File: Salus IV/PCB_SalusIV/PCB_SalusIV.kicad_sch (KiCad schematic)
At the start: 83 parts, among them J1 DC-005-5A-2.0, J2 DC-005-5A-2.0, Q1 IRFR5305TRPBF, Q2 IRFR5305TRPBF, Q3 IRFR5305TRPBF, Q4 IRFR5305TRPBF, Q9 IRLML6344TRPBF

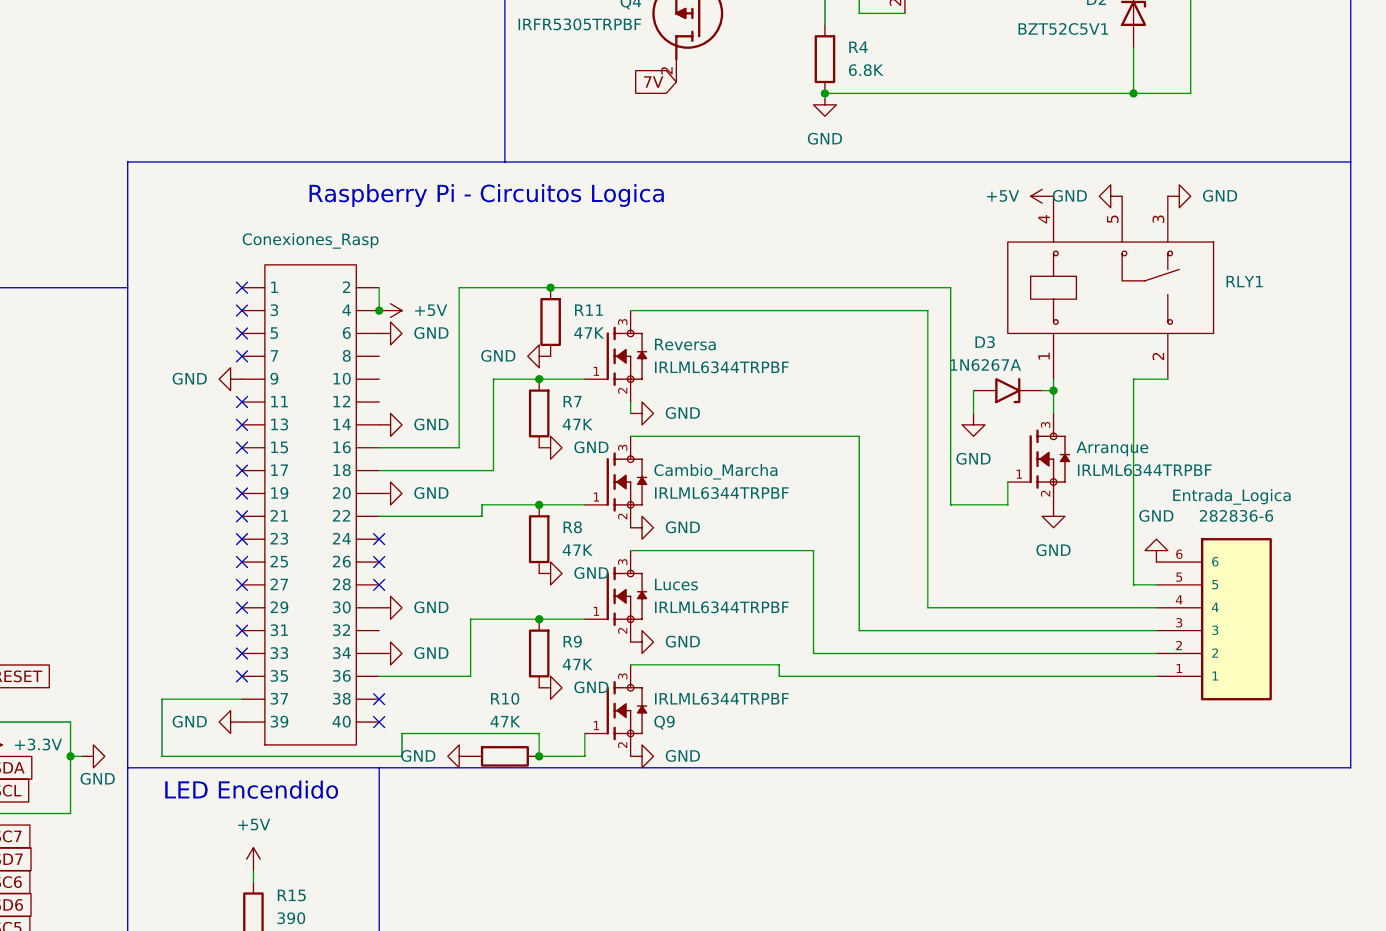
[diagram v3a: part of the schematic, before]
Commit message: Se desarrollo el esquematico de la ESP32
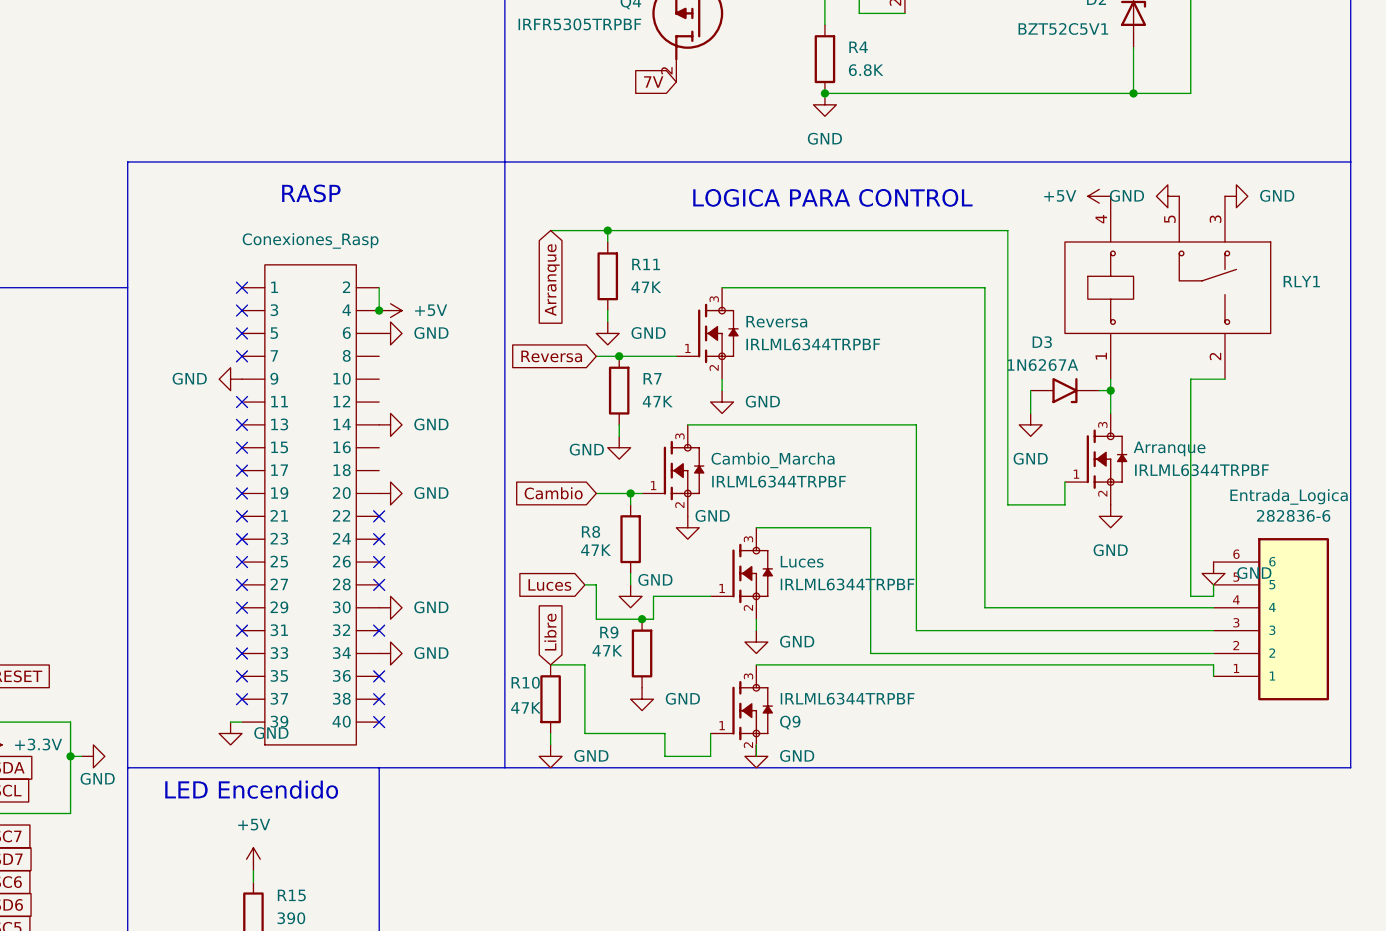
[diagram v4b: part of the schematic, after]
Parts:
- D4: LCSC PN C2286 -> C2297
- R15: LCSC PN 1206 -> C25378
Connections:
- net Libre: now reaches Q9.1, R10.1
- net Libre: no longer Conexiones_Rasp.37
- net Arranque: now reaches Arranque.1, R11.2
- net Arranque: no longer Conexiones_Rasp.16
- net Reversa: now reaches R7.2, Reversa.1
- net Reversa: no longer Conexiones_Rasp.18
- net Luces: now reaches Luces.1, R9.2
- net Luces: no longer Conexiones_Rasp.36
- net Cambio: now reaches Cambio_Marcha.1, R8.2
- net Cambio: no longer Conexiones_Rasp.22
- no-connect marks 29 -> 33
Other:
- note added: "LOGICA PARA CONTROL"
- note added: "RASP"
- note removed: "Raspberry Pi - Circuitos Logica"
- moved on the sheet: Arranque, Cambio_Marcha, D3, Entrada_Logica, Luces, Q9, R10, R11, R7, R8, R9, RLY1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

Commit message: Se agregan cambios antes de agregar arrays
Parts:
- removed Q9: IRLML6344TRPBF, Footprints:TRANS_IRLML6344TRPBF, symbol Simbolos:IRLML6344TRPBF
- removed R10: 47K, Resistor_SMD:R_1206_3216Metric, symbol Device:R
- added Acelerador1: ~, Footprints:CONN-TH_2P-P5.00_CPC3703CTR, symbol Simbolos:WJ127-5.0-2P
- added Alimentacion-Ultra1: ~, Footprints:HDR-TH_16P-P2.54-V-M-R2-C8-S2.54, symbol Simbolos:Header-Male-2.54_2x8
- added Conectores-Carreras1, Conectores-Giro1: ~, Footprints:CONN-TH_S4B-XH-A-LF-SN, symbol Simbolos:S4B-XH-A (LF)(SN)
- added Conectores-Hall1: ~, Footprints:CONN-TH_S3B-XH-A-LF-SN, symbol Simbolos:S3B-XH-A (LF)(SN)
- added Conectores-Motor1: ~, Footprints:HDR-TH_6P-P2.54-V-M-R2-C3-S2.54-1, symbol Simbolos:Header-Male-2.54_2x3
- added J3: RC, Connector_PinHeader_2.54mm:PinHeader_1x03_P2.54mm_Vertical, symbol Connector:Conn_01x03_Pin
- Entrada_Logica: footprint 282836-6:TE_282836-6 -> Footprints:TE_282836-6
- R13: footprint (none) -> Resistor_SMD:R_1206_3216Metric
- RLY1, RLY2: footprint ProLib_pcs_2026-02-12 (1):RELAY-TH_SRD-XXVDC-XL-C -> Footprints:RELAY-TH_SRD-XXVDC-XL-C
- U2: footprint ProLib_pcs_2026-02-13 (2):VQFN-24_L4.0-W4.0-P0.50-BL-EP2.5 -> Footprints:VQFN-24_L4.0-W4.0-P0.50-BL-EP2.5
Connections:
- net +5V: now also Alimentacion-Ultra1.10, Alimentacion-Ultra1.12, Alimentacion-Ultra1.14, Alimentacion-Ultra1.16, Alimentacion-Ultra1.2, Alimentacion-Ultra1.4, Alimentacion-Ultra1.6, Alimentacion-Ultra1.8, Conectores-Giro1.1, Conectores-Motor1.5, J3.3 (Pin_3); no longer Conexiones_Rasp.2, Conexiones_Rasp.4
- net GND: now also Conexiones_Rasp.25, Entrada_Logica.1, P1.1, P1.3, P2.2, P2.4, Acelerador1.2, Alimentacion-Ultra1.1, Alimentacion-Ultra1.11, Alimentacion-Ultra1.13, Alimentacion-Ultra1.15, Alimentacion-Ultra1.3, Alimentacion-Ultra1.5, Alimentacion-Ultra1.7, Alimentacion-Ultra1.9, Conectores-Carreras1.2, Conectores-Carreras1.4, Conectores-Giro1.4, Conectores-Motor1.6, J3.1 (Pin_1)
- net SC0: no longer P2.4, U2.2 (SC0)
- net SCL: no longer U2.19 (SCL)
- net SD0: no longer P2.2, U2.1 (SD0)
- net SDA: no longer U2.20 (SDA)
- net TX1: now reaches Conexiones_Rasp.10
- net RX1: now reaches Conexiones_Rasp.8
- net Expansor 1 renamed CARRERA 1
- net CARRERA 1: now also Conectores-Carreras1.1; no longer P1.1
- net Expansor 2 renamed CARRERA 2
- net CARRERA 2: now also Conectores-Carreras1.3; no longer P1.3
- new net ACELERADOR: Acelerador1.1
- new net ENABLE: Conectores-Motor1.3, Conectores-Motor1.4
- new net HALL-1: Conectores-Hall1.1
- new net HALL-2: Conectores-Hall1.2
- new net HALL-3: Conectores-Hall1.3
- new net LPWM: Conectores-Motor1.2
- new net PPM: J3.2 (Pin_2)
- new net RPWM: Conectores-Motor1.1
- new net SCL-Giro: Conectores-Giro1.3, U2.2 (SC0)
- new net SCL-MUX: U2.19 (SCL)
- new net SDA-Giro: Conectores-Giro1.2, U2.1 (SD0)
- new net SDA-MUX: U2.20 (SDA)
- no-connect marks 33 -> 37
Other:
- moved on the sheet: J3, JP1, JP10, JP11, JP12, JP13, JP14, JP15, JP16, JP17, JP18, JP2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

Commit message: Se agrega terminada antes de modificaciones de mejora
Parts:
- removed JP17, JP18: Jumper_Soldado, Jumper:SolderJumper-2_P1.3mm_Open_Pad1.0x1.5mm, symbol Jumper:SolderJumper_2_Open
- removed R12, R13, R16, R17, R18, R20, R21, R22, R23, R24, R25, R26, R27, R28, R29, R30, R31, R32, R33, R34: 4.7K, Resistor_SMD:R_1206_3216Metric, symbol Device:R
- added C9: 100nF, Capacitor_SMD:C_0603_1608Metric, symbol Device:C
- added H1, H2, H3: MountingHole, MountingHole:MountingHole_3.2mm_M3, symbol Mechanical:MountingHole
- added R10, R18: 4.7kΩ, Footprints:RES-ARRAY-SMD_1606-16P-L4.0-W1.6-BL, symbol Simbolos:YC248-JR-074K7L
- C1: footprint Capacitor_SMD:C_0402_1005Metric -> Capacitor_SMD:C_0603_1608Metric; LCSC PN C1525 -> C1590
- JP11: now in the parts list
- RLY1: value ~ -> Relé-Arranque
- RLY2: value ~ -> Relé-Bateria
- U1: value ~ -> MCP
- U2: value ~ -> TCA
- renumbered Alimentacion-Ultra1 to J12, Acelerador1 to J13, Conectores-Motor1 to J14, Conectores-Carreras1 to J15, Conectores-Giro1 to J16, Conectores-Hall1 to J17
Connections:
- net SCL_Expansor is gone; now on net SCL-Expansores: U1.12 (SCK)
- net SDA_Expansor is gone; now on net SDA-Expansores: U1.13 (SDA)
- net +3.3V: now also R19.2, C9.1
- net +5V: now also P2.10, P2.12, P2.14, P2.16, P2.2, P2.4, P2.6, P2.8; no longer J12.10, J12.12, J12.14, J12.16, J12.2, J12.4, J12.6, J12.8
- net Expansor 10: now also P1.14; no longer P1.4
- net Expansor 11: now also P1.12; no longer P1.6
- net Expansor 12: now also P1.10; no longer P1.8
- net Expansor 13: now also P1.8; no longer P1.10
- net Expansor 14: now also P1.6; no longer P1.12
- net Expansor 15: now also P1.4; no longer P1.14
- net Expansor 16: now also P1.2; no longer P1.16
- net Expansor 3: now also P1.15; no longer P1.5
- net Expansor 4: now also P1.13; no longer P1.7
- net Expansor 5 : now also P1.11; no longer P1.9
- net Expansor 6 : now also P1.9; no longer P1.11
- net Expansor 7 : now also P1.7; no longer P1.13
- net Expansor 8: now also P1.5; no longer P1.15
- net Expansor 9: now also P1.16; no longer P1.2
- net GND: now also P2.1, P2.3, C9.2; no longer P2.2, P2.4
- net SC1: now also J12.8, R10.10; no longer P2.8, R19.2
- net SC2: now also J12.12, R10.12; no longer P2.12
- net SC3: now also J12.16, R10.14; no longer P2.16
- net SC4: now also J12.4, R10.16; no longer P2.3
- net SC5: now also R18.16
- net SC6: now also R18.14
- net SC7: now also R18.12
- net SCL-Giro: now also R18.9
- net SD1: now also J12.6, R10.9; no longer P2.6
- net SD2: now also J12.10, R10.11; no longer P2.10
- net SD3: now also J12.14, R10.13; no longer P2.14
- net SD4: now also J12.2, R10.15; no longer P2.1
- net SD5: now also R18.15
- net SD6: now also R18.13
- net SD7: now also R18.11
- net SDA-Giro: now also R18.10
- net at JP16.2 (B): now also R10.8
- net at JP13.2 (B): now also R10.5
- net at JP3.2 (B): now also R18.5
- net at JP9.2 (B): now also R10.1
- net at JP12.2 (B): now also R10.4
- net at JP11.2 (B): now also R10.3
- net at JP5.2 (B): now also R18.7
- net at JP2.2 (B): now also R18.4
- net at RLY1.2: now also Entrada_Logica.2; no longer Entrada_Logica.5
- net at JP1.2 (B): now also R18.3
- net at JP7.2 (B): now also R18.1
- net at JP4.2 (B): now also R18.6
- net at Reversa.3: now also Entrada_Logica.5; no longer Entrada_Logica.4
- net at JP6.2 (B): now also R18.2
- net at JP14.2 (B): now also R10.6
- net at JP8.2 (B): now also R18.8
- net at Luces.3: now also Entrada_Logica.3; no longer Entrada_Logica.2
- net at Cambio_Marcha.3: now also Entrada_Logica.4; no longer Entrada_Logica.3
- net at JP15.2 (B): now also R10.7; no longer R19.1
- net at JP10.2 (B): now also R10.2
- net RESET renamed RST
- net RST: now also R19.1
- net SCL-MUX renamed SCL-Expansores
- net SDA-MUX renamed SDA-Expansores
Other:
- moved on the sheet: JP1, JP2, JP3, JP4, JP5, JP8

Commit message: Se guarda la PCB Salus IV ya terminada, queda revision final antes de envio
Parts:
- removed Arranque1: IRLML6344TRPBF, Footprints:TRANS_IRLML6344TRPBF, symbol Simbolos:IRLML6344TRPBF
- removed D5: 1N6267A, Diode_THT:D_DO-201AE_P15.24mm_Horizontal, symbol Diode:1N62xxA
- removed R35: 47K, Footprints:RES-TH_BD2.5-L6.5-P10.50-D0.6, symbol Device:R
- removed R37: 47K, Resistor_SMD:R_1206_3216Metric, symbol Device:R
- removed RLY2: Relé-Bateria, Footprints:RELAY-TH_SRD-XXVDC-XL-C, symbol Simbolos:SRD-05VDC-SL-C
- added Q10: ~, Footprints:RQ5P0, symbol Simbolos:RQ5P010SNTL
- added Q9: ~, Footprints:SI2301CDS, symbol Simbolos:SI2303CDS
- added R12: 47K, Resistor_SMD:R_1206_3216Metric, symbol Device:R
- added R13: 1K, Resistor_SMD:R_0603_1608Metric, symbol Device:R
- added R20, R21: 47K, Resistor_SMD:R_0603_1608Metric, symbol Device:R
- D3: value 1N6267A -> TPTVS0971P; footprint Diode_THT:D_DO-201AE_P15.24mm_Horizontal -> Footprints:DFN1610-2L_L1.6-W1.0-P1.10-RD; LCSC PN C1975954 -> C2923378
- R1, R6: footprint Resistor_SMD:R_1206_3216Metric -> Resistor_SMD:R_0603_1608Metric; LCSC PN C1469 -> C14676
- R11, R2, R5, R7, R8, R9: footprint Resistor_SMD:R_1206_3216Metric -> Resistor_SMD:R_0603_1608Metric; LCSC PN C25664 -> C105579
- R14: footprint Resistor_SMD:R_1206_3216Metric -> Resistor_SMD:R_0603_1608Metric; LCSC PN C1489 -> C98220
- R15: footprint Resistor_SMD:R_1206_3216Metric -> Resistor_SMD:R_0603_1608Metric; LCSC PN C25378 -> C114620
- R19: footprint Resistor_SMD:R_1206_3216Metric -> Resistor_SMD:R_0603_1608Metric; LCSC PN C26043 -> C99782
- R3, R4: footprint Resistor_SMD:R_1206_3216Metric -> Resistor_SMD:R_0603_1608Metric; LCSC PN C26046 -> C114632
- R36: footprint Footprints:RES-TH_BD1.9-L3.3-P7.30-D0.5 -> Resistor_SMD:R_1206_3216Metric; LCSC PN C58615 -> C114929
- renumbered J13 to J10, J3 to J11, J14 to J12, J15 to J5, J16 to J6, J17 to J7, J12 to J9, JP7 to JP1, JP6 to JP2
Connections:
- net +5V: now also R13.1
- net 60V: now also R12.1
- net ADC_ES: now also Q10.2 (S)
- net Arranque: now also R11.1; no longer R11.2
- net Cambio: now also R8.1; no longer R8.2
- net Control_Bat: now also Q9.1 (G), R21.1
- net GND: now also R11.2, R7.2, R8.2, R9.2, Q9.3 (D), R20.2, R21.2; no longer P2.1, P2.3, R11.1, R7.1, R8.1, R9.1
- net Luces: now also R9.1; no longer R9.2
- net Reversa: now also R7.1; no longer R7.2
- net SCL-Giro: no longer R18.9, U2.2 (SC0)
- net SDA-Giro: no longer R18.10, U2.1 (SD0)
- net at Q3.1 (G): now also R5.2; no longer R5.1
- net at D2.1 (K), R6.2: now also R5.1; no longer R5.2
- new net: Q10.1 (G), Q9.2 (S), R13.2, R20.1
- new net: Q10.3 (D), R12.2
- new net SC0: P2.3, R18.9, U2.2 (SC0)
- new net SD0: P2.1, R18.10, U2.1 (SD0)
- no-connect marks 37 -> 36
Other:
- moved on the sheet: P3, R36
